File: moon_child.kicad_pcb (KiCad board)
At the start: 4 copper layers, 175 parts, among them J1 Conn_01x06, J2 Conn_01x06, J3 Conn_01x04, J4 Micro_SD_Card_Det1, J5 Conn_01x04, J6 Conn_01x04, J7 Conn_02x05_Odd_Even, J8 Conn_01x03, J9 debug_probe, Q1 BSP613P, SW1 SW_Omron_B3FS, U1 DRV8871DDA, U2 DRV8871DDA, U3 AP62250Z6, U4 IIM-42652, U5 BME280, U6 RP2350B-QFN80, U7 INA180A1, U8 16Mbit PSRAM, X1 ASE-12.000MHZ-L-C-T

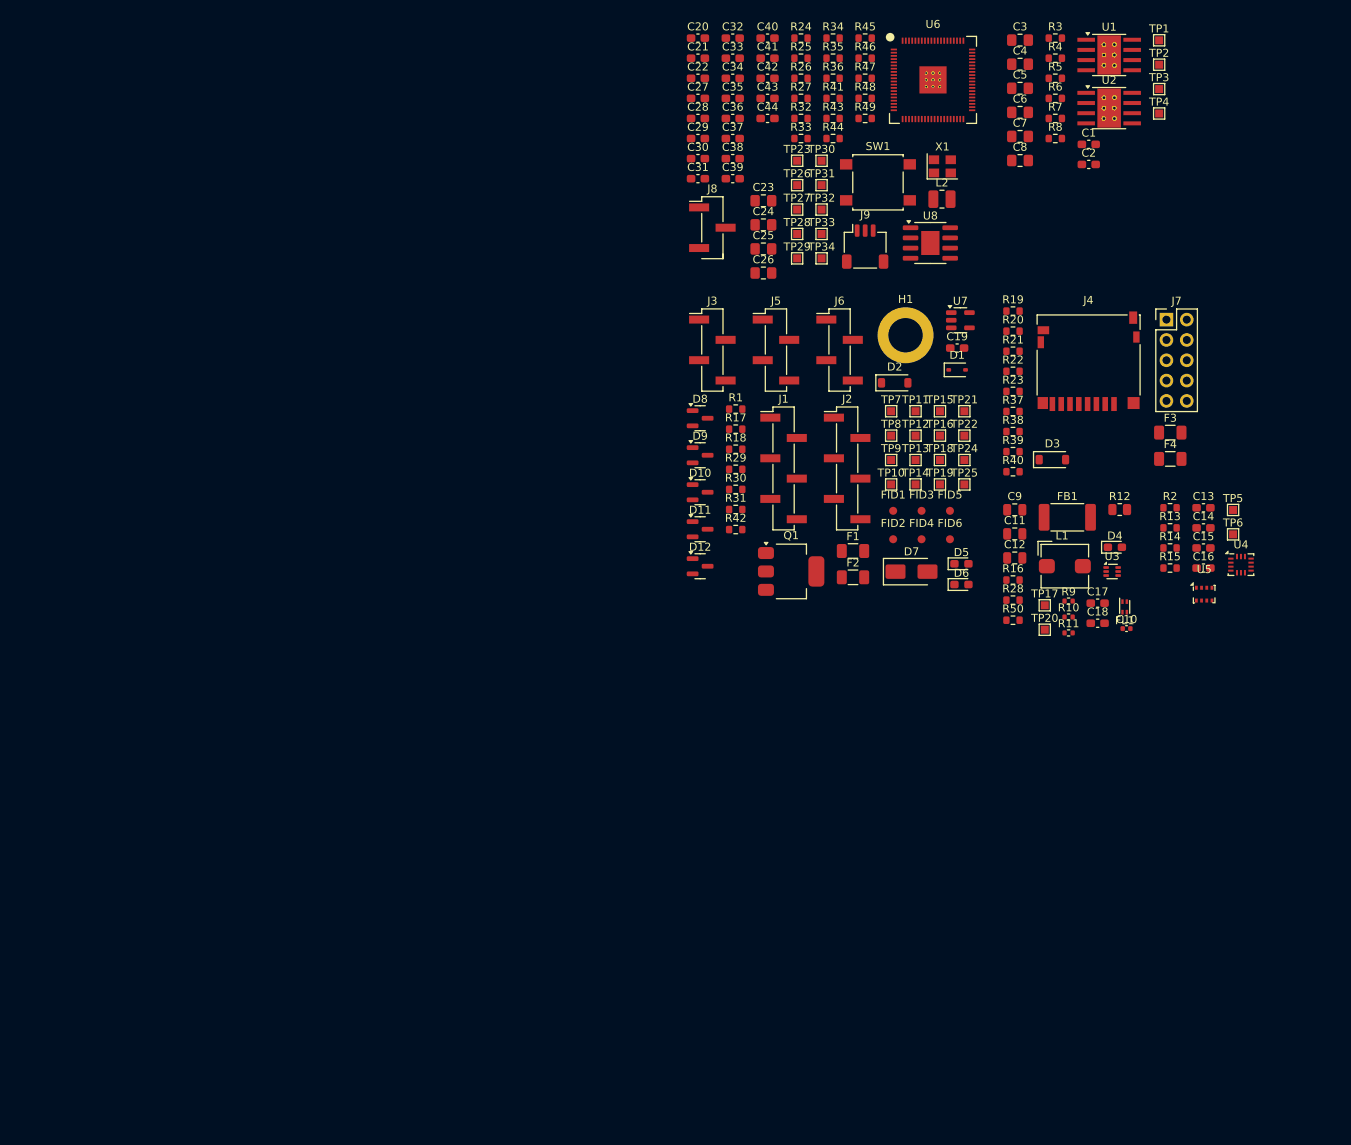
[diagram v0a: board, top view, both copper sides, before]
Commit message: footprint cleanup
switched to 0402 resistors, updated connectors, etc...
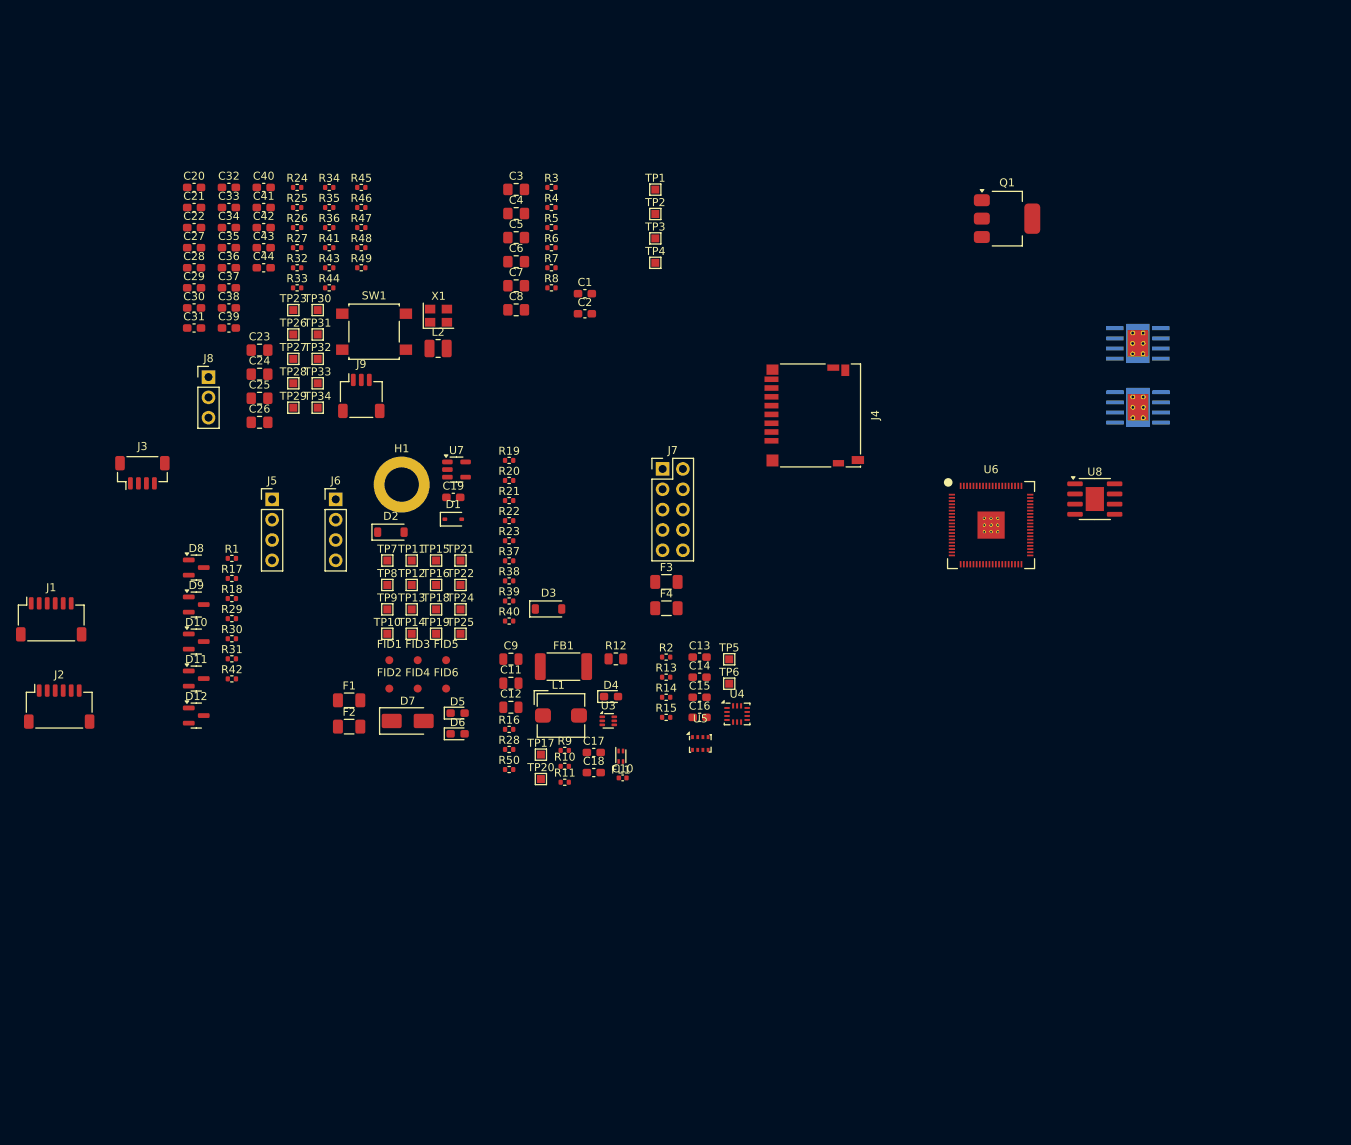
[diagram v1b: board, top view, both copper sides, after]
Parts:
- J1: value Conn_01x06 -> Motor0; footprint Connector_PinHeader_2.54mm:PinHeader_1x06_P2.54mm_Vertical_SMD_Pin1Left -> Connector_JST:JST_SH_SM06B-SRSS-TB_1x06-1MP_P1.00mm_Horizontal
- J2: value Conn_01x06 -> Motor1; footprint Connector_PinHeader_2.54mm:PinHeader_1x06_P2.54mm_Vertical_SMD_Pin1Left -> Connector_JST:JST_SH_SM06B-SRSS-TB_1x06-1MP_P1.00mm_Horizontal
- J3: value Conn_01x04 -> Battery Input; footprint Connector_PinHeader_2.54mm:PinHeader_1x04_P2.54mm_Vertical_SMD_Pin1Left -> Connector_JST:JST_SH_BM04B-SRSS-TB_1x04-1MP_P1.00mm_Vertical
- J5, J6: footprint Connector_PinHeader_2.54mm:PinHeader_1x04_P2.54mm_Vertical_SMD_Pin1Left -> Connector_PinHeader_2.54mm:PinHeader_1x04_P2.54mm_Vertical
- J8: footprint Connector_PinHeader_2.54mm:PinHeader_1x03_P2.54mm_Vertical_SMD_Pin1Left -> Connector_PinHeader_2.54mm:PinHeader_1x03_P2.54mm_Vertical
- R1, R13, R14, R15, R16, R17, R18, R19, R2, R20, R21, R22, R23, R24, R25, R26, R27, R28, R29, R3, R30, R31, R32, R33, R34, R35, R36, R37, R38, R39, R4, R40, R41, R42, R43, R44, R45, R46, R47, R48, R49, R5, R50, R6, R7, R8: footprint Resistor_SMD:R_0603_1608Metric -> Resistor_SMD:R_0402_1005Metric
- U1, U2: moved to B.Cu
- moved J2 102.9 mm to (41.4, 124.7)
- moved J1 93.5 mm to (40.4, 113.8)
- moved J3 72.9 mm to (51.8, 95.5)
- moved C1 65.7 mm to (107.1, 73.1)
- moved C10 65.7 mm to (111.8, 133.6)
- moved C11 65.7 mm to (97.9, 121.8)
- moved C12 65.7 mm to (97.9, 124.8)
- moved C2 65.7 mm to (107.1, 75.6)
- moved C9 65.7 mm to (97.9, 118.8)
- moved D7 65.7 mm to (85.0, 126.5)
- moved F1 65.7 mm to (77.7, 123.9)
- moved F2 65.7 mm to (77.7, 127.2)
- moved F3 65.7 mm to (117.3, 109.1)
- moved F4 65.7 mm to (117.3, 112.4)
- moved R16 65.7 mm to (97.7, 127.5)
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
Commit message: Added USB C Connector
Added usb C connector, consolidated ESD parts, cleaned up footprint selection.
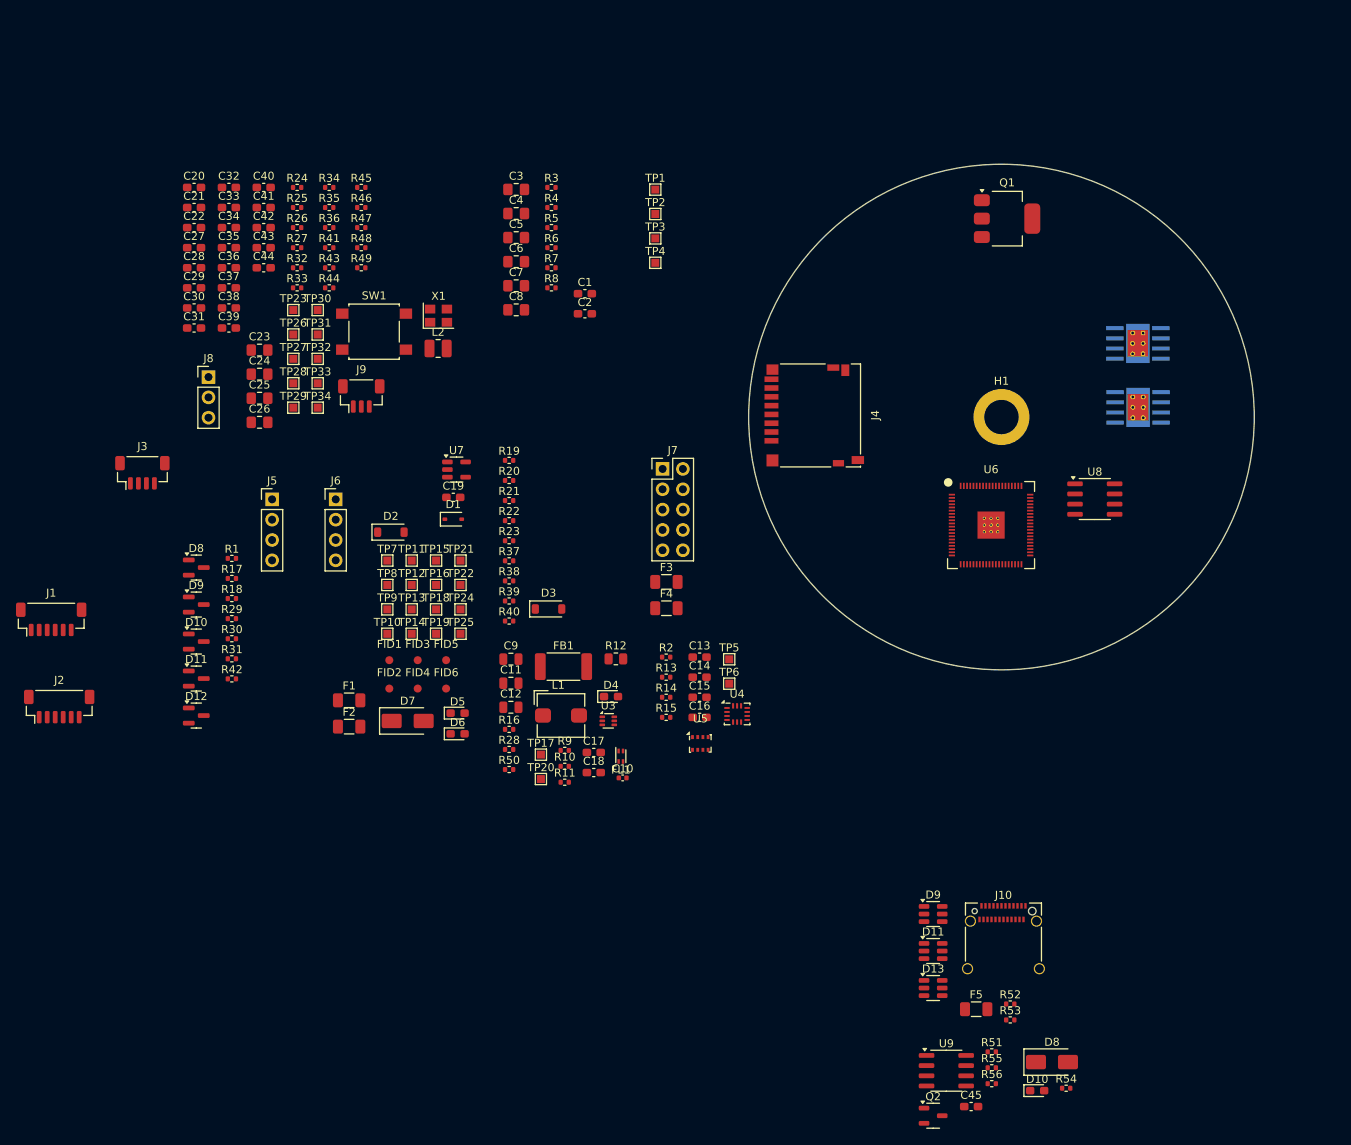
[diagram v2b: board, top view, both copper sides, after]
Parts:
- added C45: 0.1u, Capacitor_SMD:C_0603_1608Metric_Pad1.08x0.95mm_HandSolder, F.Cu at (155.4, 174.7)
- added D10: LED, Diode_SMD:D_0603_1608Metric_Pad1.05x0.95mm_HandSolder, F.Cu at (163.7, 172.7)
- added D11: ESDA6V1BC6, Package_TO_SOT_SMD:SOT-23-6, F.Cu at (150.7, 155.2)
- added D13: ESDA6V1BC6, Package_TO_SOT_SMD:SOT-23-6, F.Cu at (150.7, 159.9)
- added D8: D, Diode_SMD:D_SMA, F.Cu at (165.5, 169.1)
- added D9: ESDA6V1BC6, Package_TO_SOT_SMD:SOT-23-6, F.Cu at (150.7, 150.6)
- added F5: 500mA, Fuse:Fuse_1206_3216Metric, F.Cu at (156.0, 162.5)
- added J10: USB_C_Receptacle_USB2.0_14P, Connector_USB:USB_C_Receptacle_Amphenol_12401610E4-2A_CircularHoles, F.Cu at (159.4, 154.6)
- added Q2: Q_NPN_BCE, Package_TO_SOT_SMD:SOT-23-3, F.Cu at (150.7, 175.8)
- added R51: 10K, Resistor_SMD:R_0402_1005Metric, F.Cu at (158.0, 167.8)
- added R52: 5.1K, Resistor_SMD:R_0402_1005Metric, F.Cu at (160.3, 161.9)
- added R53: 5.1K, Resistor_SMD:R_0402_1005Metric, F.Cu at (160.3, 163.9)
- added R54: 3K, Resistor_SMD:R_0402_1005Metric, F.Cu at (167.3, 172.4)
- added R55: 10K, Resistor_SMD:R_0402_1005Metric, F.Cu at (158.0, 169.8)
- added R56: 10, Resistor_SMD:R_0402_1005Metric, F.Cu at (158.0, 171.8)
- added U9: 16Mbit PSRAM, Package_SO:SOIC-8_3.9x4.9mm_P1.27mm, F.Cu at (152.3, 170.2)
- J1, J2: footprint Connector_JST:JST_SH_SM06B-SRSS-TB_1x06-1MP_P1.00mm_Horizontal -> Connector_JST:JST_SH_BM06B-SRSS-TB_1x06-1MP_P1.00mm_Vertical
- J9: footprint Connector_JST:JST_SH_SM03B-SRSS-TB_1x03-1MP_P1.00mm_Horizontal -> Connector_JST:JST_SH_BM03B-SRSS-TB_1x03-1MP_P1.00mm_Vertical
- U8: footprint Package_SO:SOIC-8-1EP_3.9x4.9mm_P1.27mm_EP2.29x3mm -> Package_SO:SOIC-8_3.9x4.9mm_P1.27mm
- moved H1 75.4 mm to (159.2, 88.5)
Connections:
- net Net-(R32-Pad2) renamed /connectors+mechanical/DP+
- net Net-(R33-Pad2) renamed /connectors+mechanical/DP-
- net Net-(U6-QSPI_SCLK) renamed /raspi/QSPI_SCLK
- net Net-(U6-QSPI_SD0) renamed /raspi/QSPI_SD0
- net Net-(U6-QSPI_SD1) renamed /raspi/QSPI_SD1
- net Net-(U6-QSPI_SD2) renamed /raspi/QSPI_SD2
- net Net-(U6-QSPI_SD3) renamed /raspi/QSPI_SD3
- U6 pad 14: unconnected-(U6-GPIO15-Pad14) -> /connectors+mechanical/GPS_PPS
- U6 pad 21: unconnected-(U6-GPIO21-Pad21) -> /raspi/IMU_CLK
- U6 pad 42: /raspi/IMU_CLK -> unconnected-(U6-GPIO33-Pad42)
- U6 pad 47: unconnected-(U6-GPIO38-Pad47) -> /raspi/QSPI_BK_SS
- U6 pad 48: unconnected-(U6-GPIO39-Pad48) -> /raspi/~{USB_V_present}
- U6 pad 6: /connectors+mechanical/GPS_PPS -> unconnected-(U6-GPIO8-Pad6)
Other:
- board outline added: 63.2 x 63.2 mm

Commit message: Updated layout
Added ground fills, updated stackup, added notes.
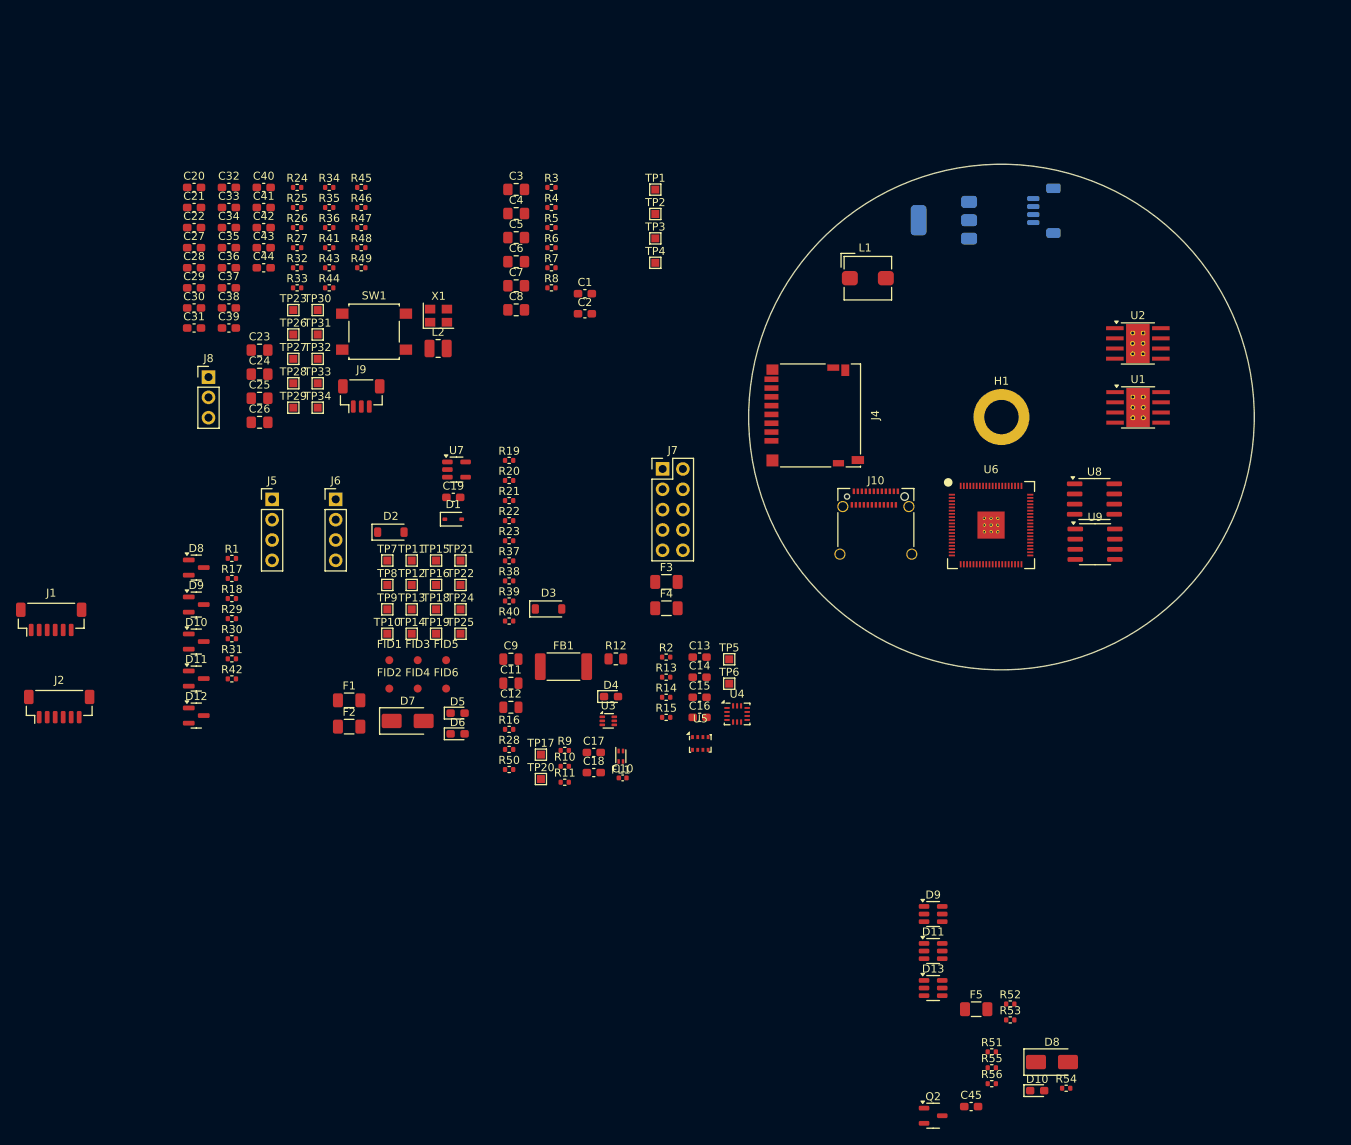
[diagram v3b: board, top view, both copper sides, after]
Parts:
- J3, Q1: moved to B.Cu
- U1, U2: moved to F.Cu
- moved J3 117.3 mm to (164.5, 62.7), turned to 90 degrees
- moved U9 68.4 mm to (170.9, 104.4)
- moved L1 66.8 mm to (142.5, 71.1)
- moved J10 54.2 mm to (143.5, 102.8)
- moved Q1 7.90 mm to (152.0, 63.9), turned to 180 degrees
- turned U1 to 0 degrees
- turned U2 to 0 degrees
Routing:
- added copper zone on In2.Cu, net 3v3
- added copper zone on In2.Cu, net Board_VBATT
- added copper zone on In1.Cu, net GND

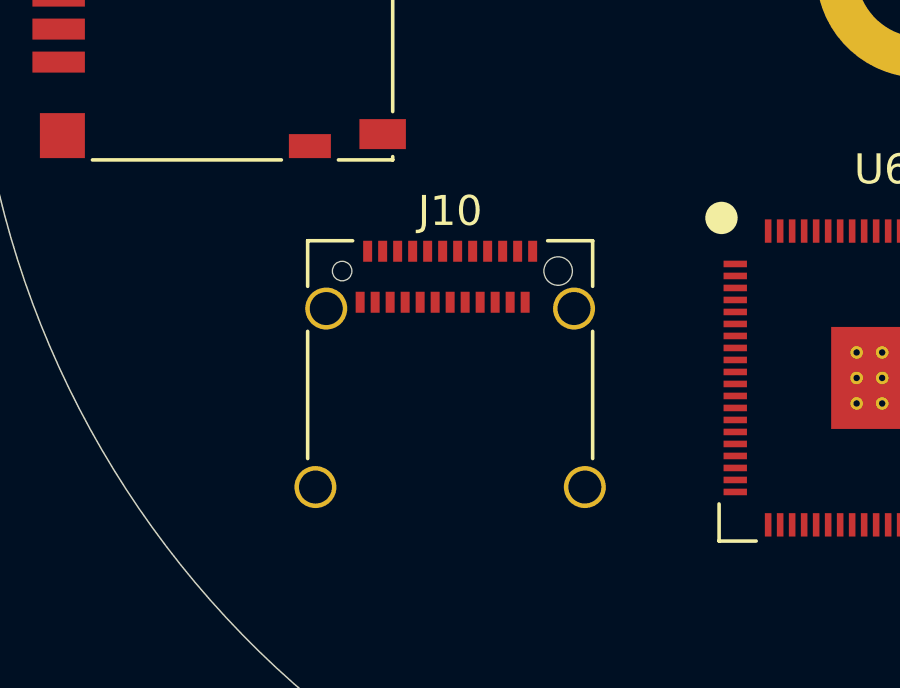
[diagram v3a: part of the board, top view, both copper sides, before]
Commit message: Swapped USB to Vert
Changed USB-C connector from horizontal to vertical
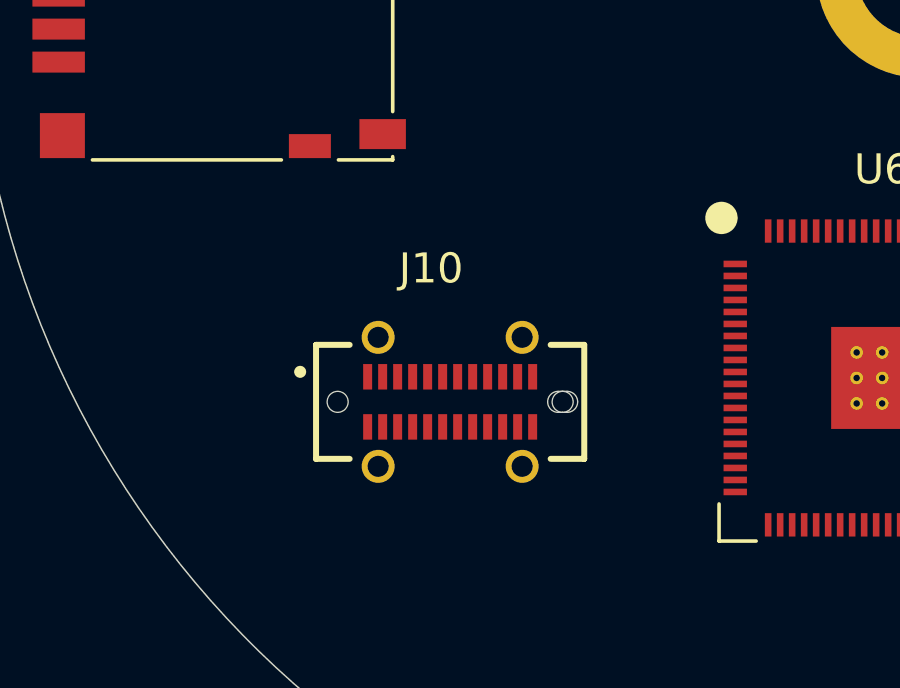
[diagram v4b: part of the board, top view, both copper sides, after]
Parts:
- J10: footprint Connector_USB:USB_C_Receptacle_Amphenol_12401610E4-2A_CircularHoles -> GCT:GCT_USB4115-03-C_REVB4
